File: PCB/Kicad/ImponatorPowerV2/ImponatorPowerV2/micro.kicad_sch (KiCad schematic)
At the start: 7 parts, among them U2 EFM8UB10F16G

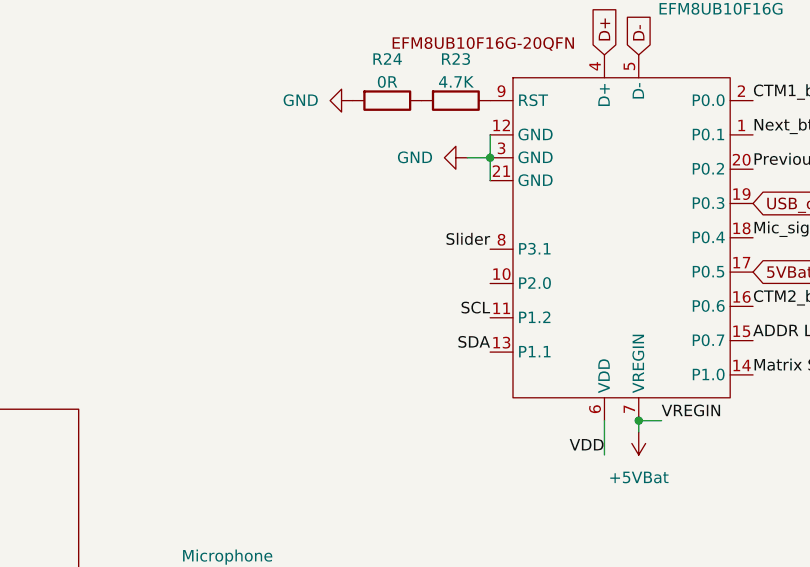
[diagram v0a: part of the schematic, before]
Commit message: PCB routed, not ready for production
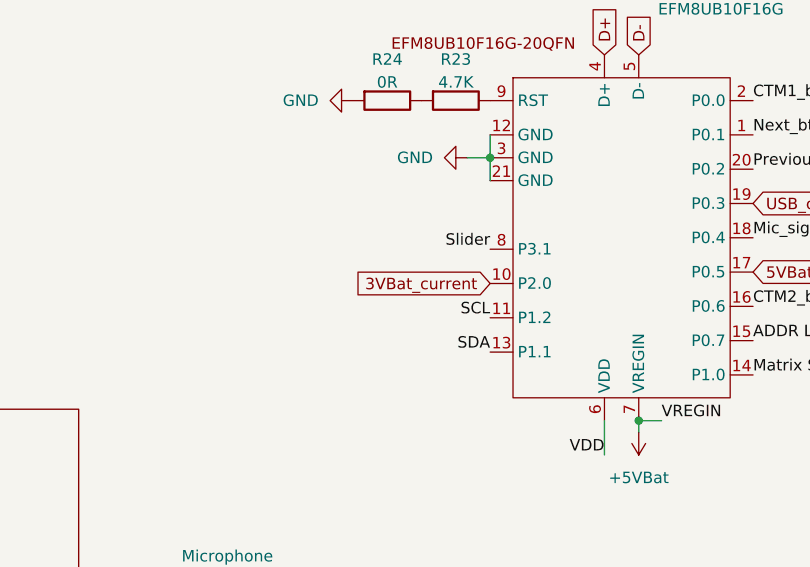
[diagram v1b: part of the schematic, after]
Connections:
- net 3VBat_current: now reaches U2.10 (P2.0)
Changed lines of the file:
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@@
+		)
+	)
+	(global_label "3VBat_current"
+		(shape input)
+		(at 139.7 87.63 180)
+		(fields_autoplaced yes)
+		(effects
+			(font
+				(size 1.27 1.27)
+			)
+			(justify right)
+		)
+		(property "Intersheetrefs" "${INTERSHEET_REFS}"
+			(at 123.5311 87.63 0)
+			(effects
+				(font
+					(size 1.27 1.27)
+				)
+				(justify right)
+				(hide yes)
+			)
 		)
 	)
